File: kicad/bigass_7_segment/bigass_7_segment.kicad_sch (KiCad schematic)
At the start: 37 parts, among them J1 Conn_01x02, J2 Conn_01x02, J3 Conn_01x02, J4 Conn_01x02, J5 Conn_01x01, J6 Conn_01x01, J7 Conn_01x01, J8 Conn_01x01, Q3 25V 1.5A

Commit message: Bigass 7 segment display rev B
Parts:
- D1, D10, D11, D12, D14, D15, D16, D17, D18, D19, D2, D3, D4, D5, D6, D7, D8, D9: symbol lib_sch:LED_RGB_Mirrored -> Custom_LED:LED_RGB_AAAKKK; LCSC_MPN (none) -> C516304; Standard Cost (none) -> 0.02
- D13: LCSC_MPN (none) -> C22624
- GRAPHIC1: symbol lib_sch:Graphic -> Custom_Placeholder:Graphic
- J1, J2, J3, J4, J5, J6, J7, J8: now left out of the parts list
- Q3: LCSC_MPN (none) -> C181160
- R1: footprint Resistor_SMD:R_0603_1608Metric -> Resistor_SMD:R_0805_2012Metric; LCSC_MPN (none) -> C84376; MPN AF0603JR-0710K -> RC0805FR-0710KL; Standard Cost (none) -> 0.01
- R2: LCSC_MPN (none) -> C137582; MPN (none) -> RC0805FR-071K3L; Standard Cost (none) -> 0.01
- R3, R4, R5: LCSC_MPN (none) -> C137529; MPN (none) -> RC0805FR-073R9L; Standard Cost (none) -> 0.01

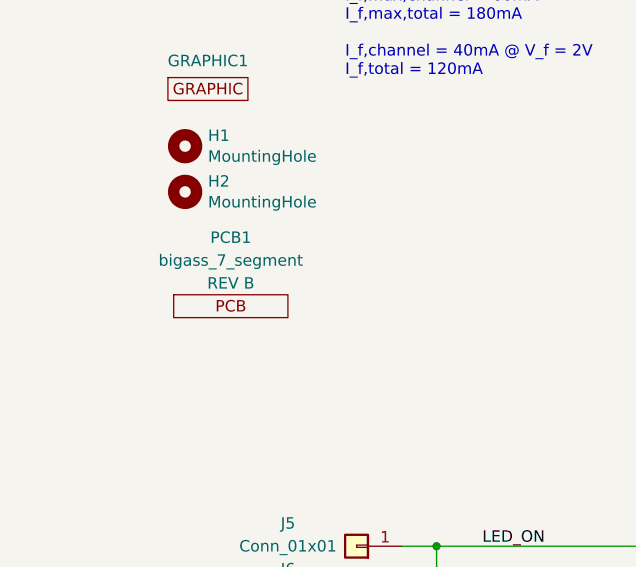
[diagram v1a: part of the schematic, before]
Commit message: Add demo mode to display code
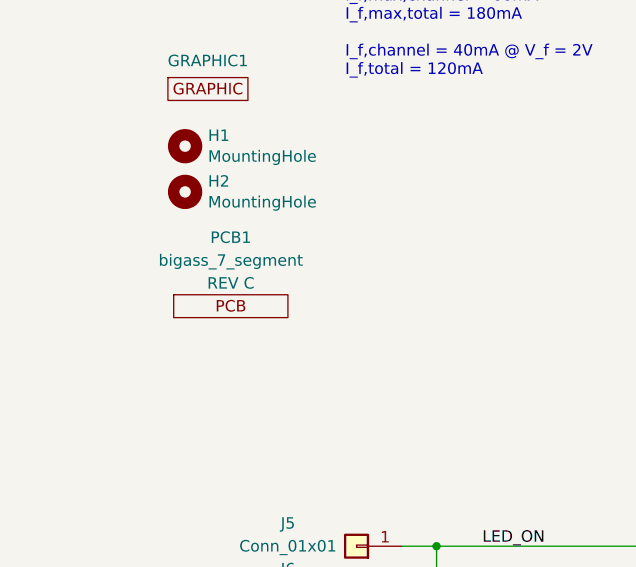
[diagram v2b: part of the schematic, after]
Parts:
- H1, H2: footprint MountingHole:MountingHole_3mm -> Custom_MountingHole:MountingHole_3.2mm_M3_Isolated
- PCB1: REV REV B -> REV C
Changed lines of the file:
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@@
   (title_block
     (title "Bigass 7 Segment Display")
-    (date "2023-06-29")
-    (rev "B")
+    (date "2023-07-06")
+    (rev "C")
     (company "Pants for Birds")
     (comment 1 "John McNelly - jkailimcnelly@gmail.com")
@@
       (effects (font (size 1.27 1.27)) (justify left))
     )
-    (property "Footprint" "MountingHole:MountingHole_3mm" (at 50.8 107.95 0)
+    (property "Footprint" "Custom_MountingHole:MountingHole_3.2mm_M3_Isolated" (at 50.8 107.95 0)
       (effects (font (size 1.27 1.27)) hide)
     )
@@
       (effects (font (size 1.27 1.27)) (justify left))
     )
-    (property "Footprint" "MountingHole:MountingHole_3mm" (at 50.8 113.03 0)
+    (property "Footprint" "Custom_MountingHole:MountingHole_3.2mm_M3_Isolated" (at 50.8 113.03 0)
       (effects (font (size 1.27 1.27)) hide)
     )
@@
       (effects (font (size 1.27 1.27)))
     )
-    (property "REV" "REV B" (at 55.88 123.19 0)
-      (effects (font (size 1.27 1.27)))
-    )
+    (property "REV" "REV C" (at 55.88 123.19 0)
+      (effects (font (size 1.27 1.27)))
+    )
